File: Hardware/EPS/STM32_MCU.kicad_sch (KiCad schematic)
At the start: 3 parts

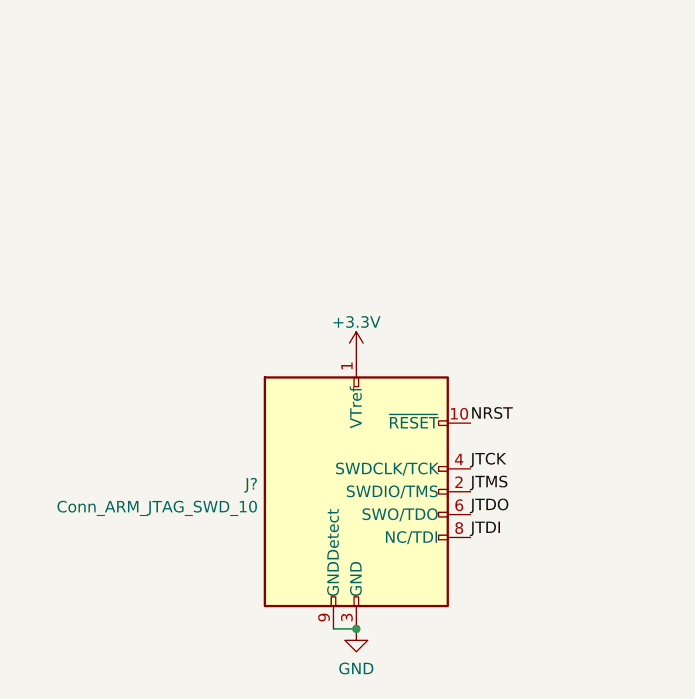
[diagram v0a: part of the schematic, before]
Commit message: Added Power sheet and ESD Protection
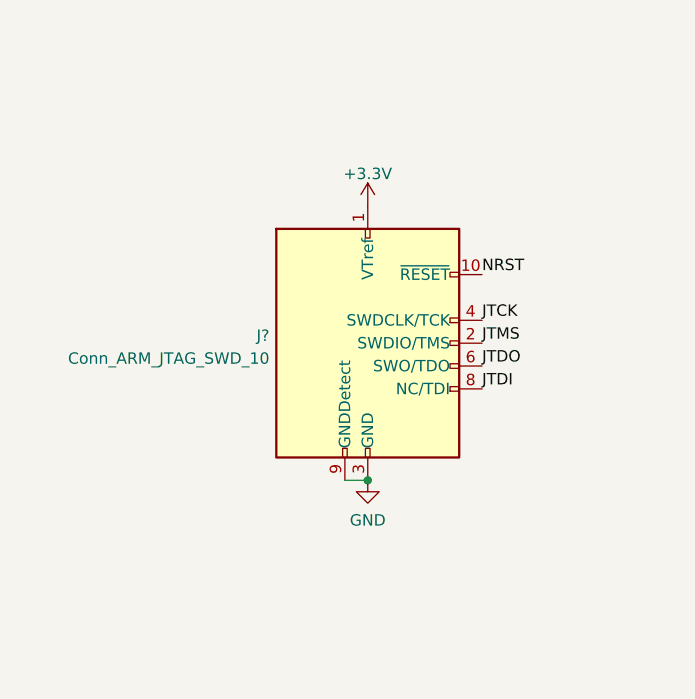
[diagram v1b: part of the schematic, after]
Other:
- moved on the sheet: J?
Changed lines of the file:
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@@
   (junction (at 198.12 22.86) (diameter 0) (color 0 0 0 0)
   )
-  (junction (at 66.04 182.88) (diameter 0) (color 0 0 0 0)
+  (junction (at 67.31 166.37) (diameter 0) (color 0 0 0 0)
   )
   (junction (at 200.66 22.86) (diameter 0) (color 0 0 0 0)
@@
     (stroke (width 0) (type default) (color 0 0 0 0))
   )
-  (wire (pts (xy 63.5 182.88) (xy 66.04 182.88))
+  (wire (pts (xy 64.77 166.37) (xy 67.31 166.37))
     (stroke (width 0) (type default) (color 0 0 0 0))
   )
@@
     (effects (font (size 1.27 1.27)) (justify left bottom))
   )
-  (label "JTCK" (at 78.74 165.1 0)
+  (label "JTCK" (at 80.01 148.59 0)
     (effects (font (size 1.27 1.27)) (justify left bottom))
   )
@@
     (effects (font (size 1.27 1.27)) (justify right bottom))
   )
-  (label "NRST" (at 78.74 160.02 0)
-    (effects (font (size 1.27 1.27)) (justify left bottom))
-  )
-  (label "JTMS" (at 78.74 167.64 0)
-    (effects (font (size 1.27 1.27)) (justify left bottom))
-  )
-  (label "JTDO" (at 78.74 170.18 0)
+  (label "NRST" (at 80.01 143.51 0)
+    (effects (font (size 1.27 1.27)) (justify left bottom))
+  )
+  (label "JTMS" (at 80.01 151.13 0)
+    (effects (font (size 1.27 1.27)) (justify left bottom))
+  )
+  (label "JTDO" (at 80.01 153.67 0)
     (effects (font (size 1.27 1.27)) (justify left bottom))
   )
@@
     (effects (font (size 1.27 1.27)) (justify right bottom))
   )
-  (label "JTDI" (at 78.74 172.72 0)
+  (label "JTDI" (at 80.01 156.21 0)
     (effects (font (size 1.27 1.27)) (justify left bottom))
   )
@@
     (effects (font (size 1.27 1.27)) (justify right))
   )
-  (symbol (lib_id "Connector:Conn_ARM_JTAG_SWD_10") (at 66.04 167.64 0) (unit 1)
-    (in_bom yes) (on_board yes) (fields_autoplaced)
-    (property "Reference" "J?" (id 0) (at 55.118 166.8053 0)
+  (symbol (lib_id "Connector:Conn_ARM_JTAG_SWD_10") (at 67.31 151.13 0) (unit 1)
+    (in_bom yes) (on_board yes) (fields_autoplaced)
+    (property "Reference" "J?" (id 0) (at 56.388 150.2953 0)
       (effects (font (size 1.27 1.27)) (justify right))
     )
-    (property "Value" "Conn_ARM_JTAG_SWD_10" (id 1) (at 55.118 169.3422 0)
+    (property "Value" "Conn_ARM_JTAG_SWD_10" (id 1) (at 56.388 152.8322 0)
       (effects (font (size 1.27 1.27)) (justify right))
     )
-    (property "Footprint" "" (id 2) (at 66.04 167.64 0)
-      (effects (font (size 1.27 1.27)) hide)
-    )
-    (property "Datasheet" "http://infocenter.arm.com/help/topic/com.arm.doc.ddi0314h/DDI0314H_coresight_components_trm.pdf" (id 3) (at 57.15 199.39 90)
+    (property "Footprint" "" (id 2) (at 67.31 151.13 0)
+      (effects (font (size 1.27 1.27)) hide)
+    )
+    (property "Datasheet" "http://infocenter.arm.com/help/topic/com.arm.doc.ddi0314h/DDI0314H_coresight_components_trm.pdf" (id 3) (at 58.42 182.88 90)
       (effects (font (size 1.27 1.27)) hide)
     )
@@
     (pin "9")
   )
-  (symbol (lib_id "power:GND") (at 66.04 182.88 0) (unit 1)
-    (in_bom yes) (on_board yes) (fields_autoplaced)
-    (property "Reference" "#PWR?" (id 0) (at 66.04 189.23 0)
-      (effects (font (size 1.27 1.27)) hide)
-    )
-    (property "Value" "GND" (id 1) (at 66.04 187.3234 0))
-    (property "Footprint" "" (id 2) (at 66.04 182.88 0)
-      (effects (font (size 1.27 1.27)) hide)
-    )
-    (property "Datasheet" "" (id 3) (at 66.04 182.88 0)
+  (symbol (lib_id "power:GND") (at 67.31 166.37 0) (unit 1)
+    (in_bom yes) (on_board yes) (fields_autoplaced)
+    (property "Reference" "#PWR?" (id 0) (at 67.31 172.72 0)
+      (effects (font (size 1.27 1.27)) hide)
+    )
+    (property "Value" "GND" (id 1) (at 67.31 170.8134 0))
+    (property "Footprint" "" (id 2) (at 67.31 166.37 0)
+      (effects (font (size 1.27 1.27)) hide)
+    )
+    (property "Datasheet" "" (id 3) (at 67.31 166.37 0)
       (effects (font (size 1.27 1.27)) hide)
     )
@@
     (pin "1")
   )
-  (symbol (lib_id "power:+3.3V") (at 66.04 152.4 0) (unit 1)
-    (in_bom yes) (on_board yes) (fields_autoplaced)
-    (property "Reference" "#PWR?" (id 0) (at 66.04 156.21 0)
-      (effects (font (size 1.27 1.27)) hide)
-    )
-    (property "Value" "+3.3V" (id 1) (at 66.04 148.8242 0))
-    (property "Footprint" "" (id 2) (at 66.04 152.4 0)
-      (effects (font (size 1.27 1.27)) hide)
-    )
-    (property "Datasheet" "" (id 3) (at 66.04 152.4 0)
-      (effects (font (size 1.27 1.27)) hide)
-    )
+  (symbol (lib_id "power:+3.3V") (at 67.31 135.89 0) (unit 1)
+    (in_bom yes) (on_board yes) (fields_autoplaced)
+    (property "Reference" "#PWR?" (id 0) (at 67.31 139.7 0)
+      (effects (font (size 1.27 1.27)) hide)
+    )
+    (property "Value" "+3.3V" (id 1) (at 67.31 132.3142 0))
+    (property "Footprint" "" (id 2) (at 67.31 135.89 0)
+      (effects (font (size 1.27 1.27)) hide)
+    )
+    (property "Datasheet" "" (id 3) (at 67.31 135.89 0)
+      (effects (font (size 1.27 1.27)) hide)
+    )
